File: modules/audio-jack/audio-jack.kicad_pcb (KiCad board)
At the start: 2 copper layers, 19.4 x 19.5 mm, 6 parts, among them J1 SJ-43514-SMT-TR

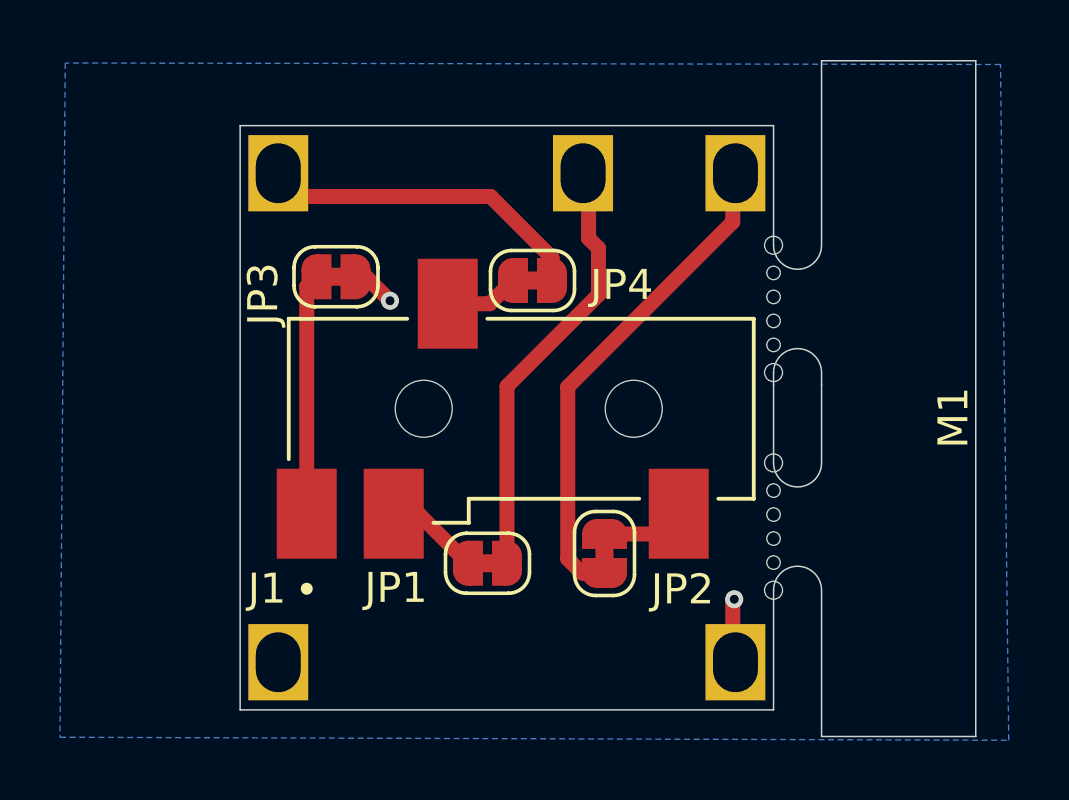
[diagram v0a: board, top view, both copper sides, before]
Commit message: KiCad v9 adding new footprints
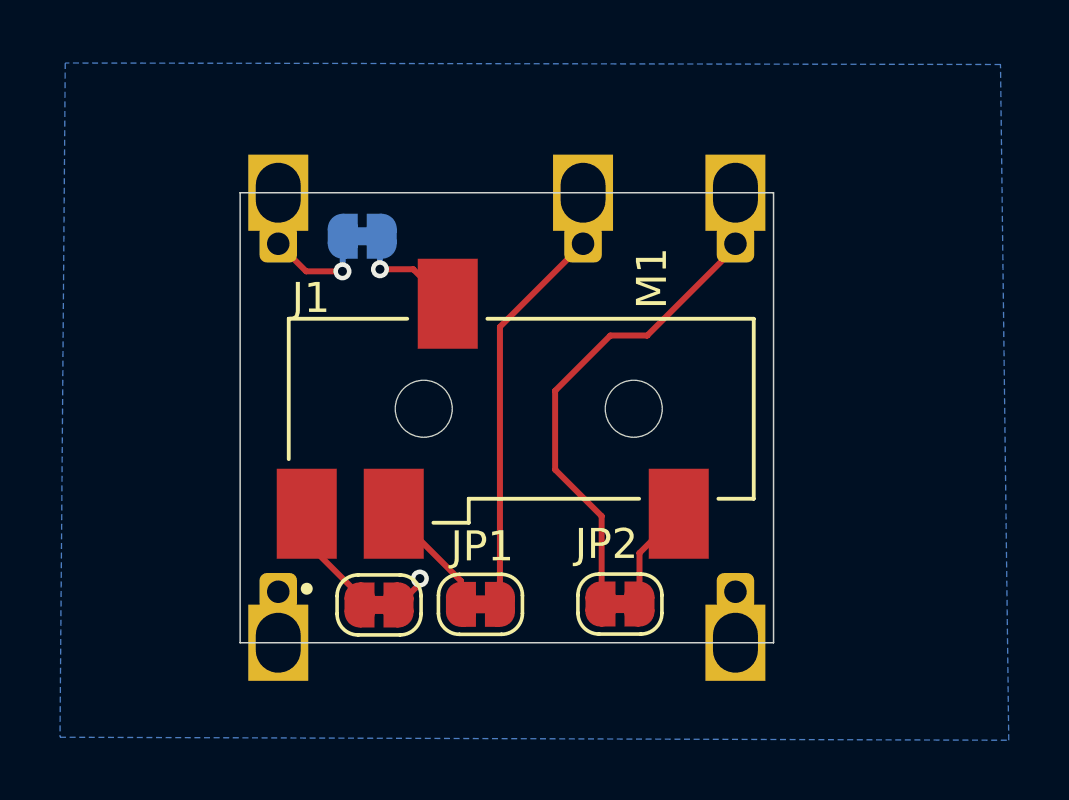
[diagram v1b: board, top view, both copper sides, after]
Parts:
- JP4: moved to B.Cu
- M1: footprint MegaCastle:MegaCastle2x7-Module-I12.7x13.0-M8314-PANEL-NIBBLE -> MegaCastle:MegaCastle2x7-Module-I15.0x13.0-M8314-SPAREPAD
- moved JP3 11.0 mm to (43.0, 43.0)
- moved JP4 5.86 mm to (42.5, 30.8), turned to 0 degrees
- moved JP2 1.76 mm to (51.0, 43.0), turned to 0 degrees
- moved JP1 1.39 mm to (46.4, 43.0)
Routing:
- net LEFT: track 11.2 -> 3.70 mm, vias 0 -> 1
- net Net-(JP3-A): track 8.03 -> 3.77 mm
- net GND: track 3.78 -> 1.17 mm, vias 2 -> 1
- net Net-(JP4-B): track 2.50 -> 3.86 mm, vias 0 -> 1
- net MIC: track 14.4 -> 13.2 mm
- net Net-(JP2-B): track 2.75 -> 3.55 mm
- net Net-(JP1-A): track 3.16 -> 3.95 mm
- net RIGHT: track 16.6 -> 15.9 mm
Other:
- board size 19.4 x 19.5 mm -> 17.8 x 15 mm
